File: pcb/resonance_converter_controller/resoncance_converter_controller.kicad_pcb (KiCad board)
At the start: 2 copper layers, 61.4 x 94 mm, 232 parts, among them J1 Micro_SD_Card_Det2, J2 USB_C_Receptacle_USB2.0_14P, J3 FX18-120P-0.8SV, J7 Conn_ARM_SWD_TagConnect_TC2030, Q1 FDMC8032L, Q2 FDMC8032L, Q3 SiR696DP, SW1 SW_SPST, U1 BQ25792RQMR, U10 INA280A1xDCK, U11 INA280A1xDCK, U12 INA280A1xDCK, U13 STM32G474VEHx, U14 APS6404L-SQRx-ZR, U15 APS6404L-SQRx-ZR, U16 AT24CS32-XHM, U17 TL3116, U18 OPA2356xxDGK, U19 OPA2325, U2 TPS55289RYQR, U20 OPA356xxDBV, U3 TPS54240DRC, U4 TPS73733DCQR, U5 OPA2325, U6 LP5907MFX-3.3, U7 OPA2356xxDGK, U8 OPA356xxDBV, U9 INA280A1xDCK, Y1 16Mhz

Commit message: Update conector in som
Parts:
- removed J3: FX18-120P-0.8SV, FX18-120P-0.8SV:HIROSE_FX18-120P-0.8SV
- added C90: 100nF, Capacitor_SMD:C_0402_1005Metric, F.Cu at (229.0, 79.0)
- added C91: 10uF, Capacitor_SMD:C_1206_3216Metric, F.Cu at (223.4, 82.4)
- added C92: 100nF, Capacitor_SMD:C_0402_1005Metric, F.Cu at (229.0, 80.9)
- added C93: 100nF, Capacitor_SMD:C_0402_1005Metric, F.Cu at (229.0, 82.9)
- added D25: ESD9B3.3ST5G, Diode_SMD:D_SOD-923, F.Cu at (233.9, 73.0)
- added D26: ESD9B3.3ST5G, Diode_SMD:D_SOD-923, F.Cu at (233.9, 74.9)
- added D27: ESD9B3.3ST5G, Diode_SMD:D_SOD-923, F.Cu at (233.9, 76.9)
- added D28: ESD9B3.3ST5G, Diode_SMD:D_SOD-923, F.Cu at (233.9, 78.8)
- added D29: ESD9B3.3ST5G, Diode_SMD:D_SOD-923, F.Cu at (233.9, 80.8)
- added D30: ESD9B3.3ST5G, Diode_SMD:D_SOD-923, F.Cu at (236.6, 73.0)
- added D31: ESD9B3.3ST5G, Diode_SMD:D_SOD-923, F.Cu at (236.6, 74.9)
- added D32: ESD9B3.3ST5G, Diode_SMD:D_SOD-923, F.Cu at (236.6, 76.9)
- added D33: ESD9B3.3ST5G, Diode_SMD:D_SOD-923, F.Cu at (236.6, 78.8)
- added D34: ESD9B3.3ST5G, Diode_SMD:D_SOD-923, F.Cu at (236.6, 80.8)
- added J4: Conn_02x19_Odd_Even, Connector_PinSocket_2.54mm:PinSocket_2x19_P2.54mm_Vertical_SMD, F.Cu at (209.9, 142.6)
- added J5: Conn_01x02, Connector_AMASS:AMASS_XT30U-M_1x02_P5.0mm_Vertical, F.Cu at (193.6, 155.8)
- added J6: FX18-120S-0.8SH, FX18-120S-0.8SH:HIROSE_FX18-120S-0.8SH, B.Cu at (209.2, 149.0)
- added R67: 0R, Resistor_SMD:R_0402_1005Metric, F.Cu at (229.0, 73.0)
- added R68: 240K, Resistor_SMD:R_0402_1005Metric, F.Cu at (229.0, 75.0)
- added R69: 100K, Resistor_SMD:R_0402_1005Metric, F.Cu at (229.0, 77.0)
- added R70: R, Resistor_SMD:R_0402_1005Metric, F.Cu at (239.3, 75.0)
- added R71: R, Resistor_SMD:R_2512_6332Metric, F.Cu at (194.3, 163.8)
- added RV1: 20K, Potentiometer_SMD:Potentiometer_Bourns_3269W_Vertical, F.Cu at (236.4, 88.4)
- added U21: TPS2553DRVR, TPS2553DRVR:SON65P200X200X80-7N, F.Cu at (214.4, 92.3)
- C84: value 100nF -> 100uF; footprint Capacitor_SMD:C_0805_2012Metric -> Capacitor_SMD:C_1206_3216Metric; moved to F.Cu
- R30: value 10K -> R
- moved R30 69.2 mm to (239.3, 73.0), turned to 0 degrees
- moved C84 28.4 mm to (223.4, 75.5), turned to 0 degrees
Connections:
- net SDA renamed I2C_INT_SDA
- net VPP renamed VSYS
- C84 pad 1: VCC -> Net-(J1-VDD)
- J1 pad 4: VCC -> Net-(J1-VDD)
- R30 pad 1: Net-(U5A--) -> /Controller/AUX_PWM_CH1
- R30 pad 2: GND -> AUX_PWM_CH1
- R39 pad 1: VCC -> Net-(J1-VDD)
- R40 pad 2: VCC -> Net-(J1-VDD)
- R6 pad 1: /Power supply/VOUT_ENABLE -> /Controller/VOUT_ENABLE
- U13 pad A1: LCD_SS -> SD_SS
- U13 pad A10: SD_MOSI -> LCD_MOSI
- U13 pad A5: unconnected-(U13-PB3-PadA5) -> HRTIM_EEV9
- U13 pad A6: QSPI_BK2_IO2 -> AUX_RX
- U13 pad A7: QSPI_BK2_IO1 -> AUX_TX
- U13 pad A9: unconnected-(U13-PD1-PadA9) -> LCD_DC
- U13 pad B1: /Controller/LCD_MISO -> SD_MOSI
- U13 pad B2: unconnected-(U13-PE3-PadB2) -> ENCODER_CHB
- U13 pad B3: unconnected-(U13-PE1-PadB3) -> CTRL_RX
- U13 pad B4: unconnected-(U13-PB7-PadB4) -> SD_CARD_DETECT
- U13 pad B7: unconnected-(U13-PD2-PadB7) -> LCD_RST
- U13 pad B8: unconnected-(U13-PD0-PadB8) -> LCD_BL
- U13 pad B9: SD_SS -> LCD_SS
- U13 pad C1: unconnected-(U13-PC14-PadC1) -> /INT
- U13 pad C2: LCD_MOSI -> SD_MISO
- U13 pad C3: LCD_SCK -> SD_SCK
- U13 pad C4: unconnected-(U13-PE0-PadC4) -> CTRL_TX
- U13 pad C6: unconnected-(U13-PD3-PadC6) -> QSPI_NCS
- U13 pad C7: SD_MISO -> LCD_MISO
- U13 pad C8: SD_SCK -> LCD_SCK
- U13 pad D1: unconnected-(U13-PC15-PadD1) -> /Controller/VOUT_ENABLE
- U13 pad F1: /Analog preprocess/FB_OCD2_RECTIFIED -> QSPI_BK2_IO1
- U13 pad F4: /Analog preprocess/ISENSE_3_OUT -> /Analog preprocess/ISENSE_4_OUT
- U13 pad G1: unconnected-(U13-PC3-PadG1) -> QSPI_BK2_IO2
- U13 pad G10: unconnected-(U13-PD15-PadG10) -> GPIO3
- U13 pad G2: unconnected-(U13-PA1-PadG2) -> /Controller/AUX_PWM_CH2
- U13 pad G4: unconnected-(U13-PA0-PadG4) -> /Controller/AUX_PWM_CH1
- U13 pad G5: /Analog preprocess/ISENSE_4_OUT -> /Analog preprocess/ISENSE_2_OUT
- U13 pad G7: unconnected-(U13-PD10-PadG7) -> GPIO0
- U13 pad G8: unconnected-(U13-PD9-PadG8) -> GPIO1
- U13 pad G9: unconnected-(U13-PD13-PadG9) -> GPIO2
- U13 pad H1: QSPI_NCS -> VSENSE_IN
- U13 pad H3: /Analog preprocess/ISENSE_2_OUT -> /Analog preprocess/ISENSE_1_OUT
- U13 pad H5: LCD_BL -> GPIO4
- U13 pad H6: LCD_DC -> GPIO5
- U13 pad J10: VSENSE_IN -> /Analog preprocess/FB_OCD2_RECTIFIED
- U13 pad J2: unconnected-(U13-PA6-PadJ2) -> FAN_PWM
- U13 pad J3: CTRL_RX -> unconnected-(U13-PC5-PadJ3)
- U13 pad J4: unconnected-(U13-PB2-PadJ4) -> ENCODER_CHA
- U13 pad J6: unconnected-(U13-PE11-PadJ6) -> GPIO6
- U13 pad J8: unconnected-(U13-PB10-PadJ8) -> HRTIM_FLT3
- U13 pad K2: CTRL_TX -> unconnected-(U13-PC4-PadK2)
- U13 pad K3: /Analog preprocess/ISENSE_1_OUT -> /Analog preprocess/ISENSE_3_OUT
- U13 pad K6: LCD_RST -> GPIO7
- U2 pad 1: /Power supply/VOUT_ENABLE -> /Controller/VOUT_ENABLE

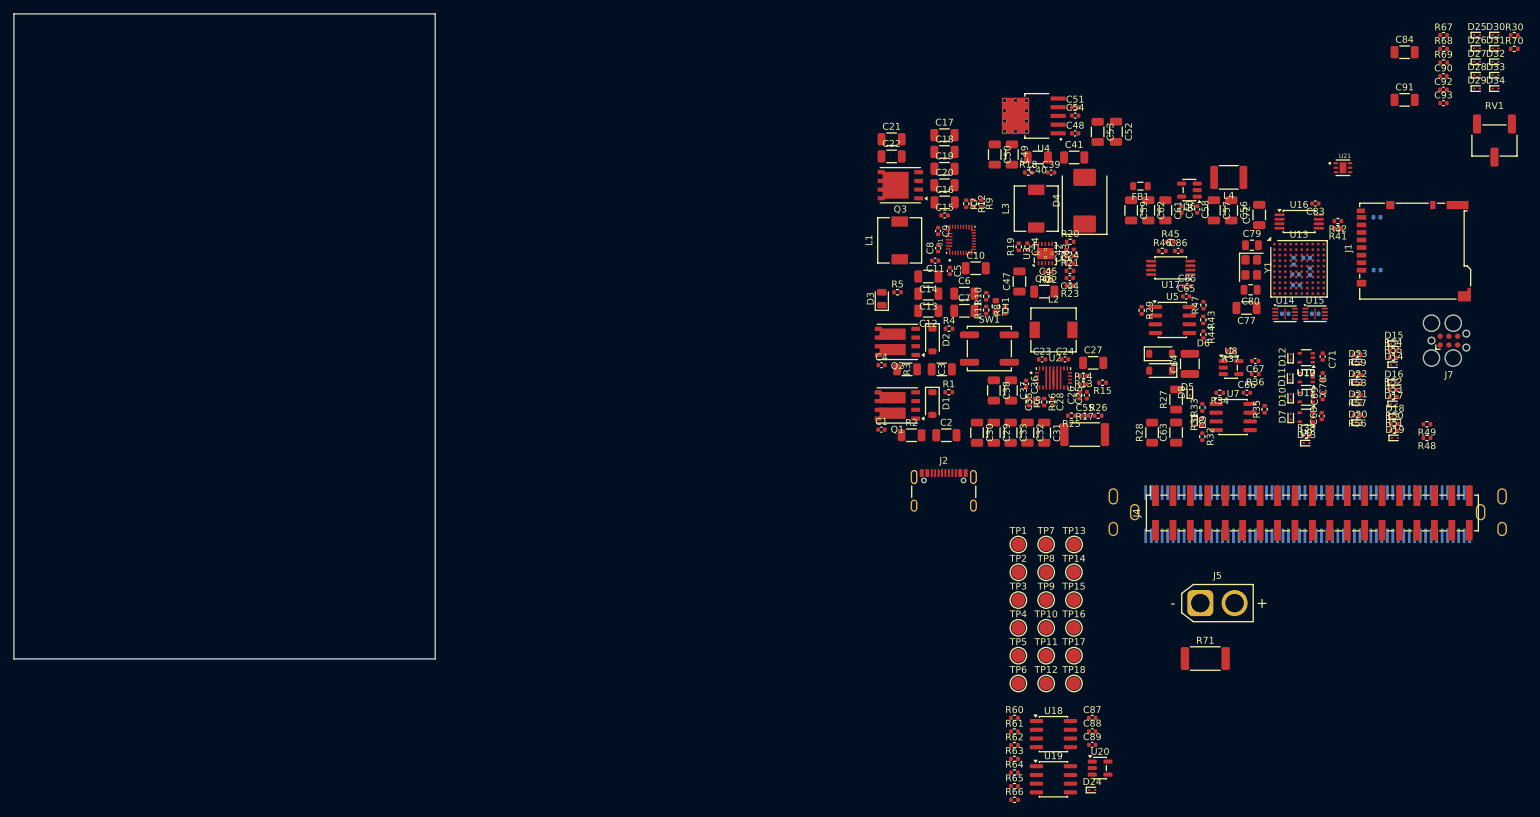
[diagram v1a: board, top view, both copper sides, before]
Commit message: First routing without testpoints
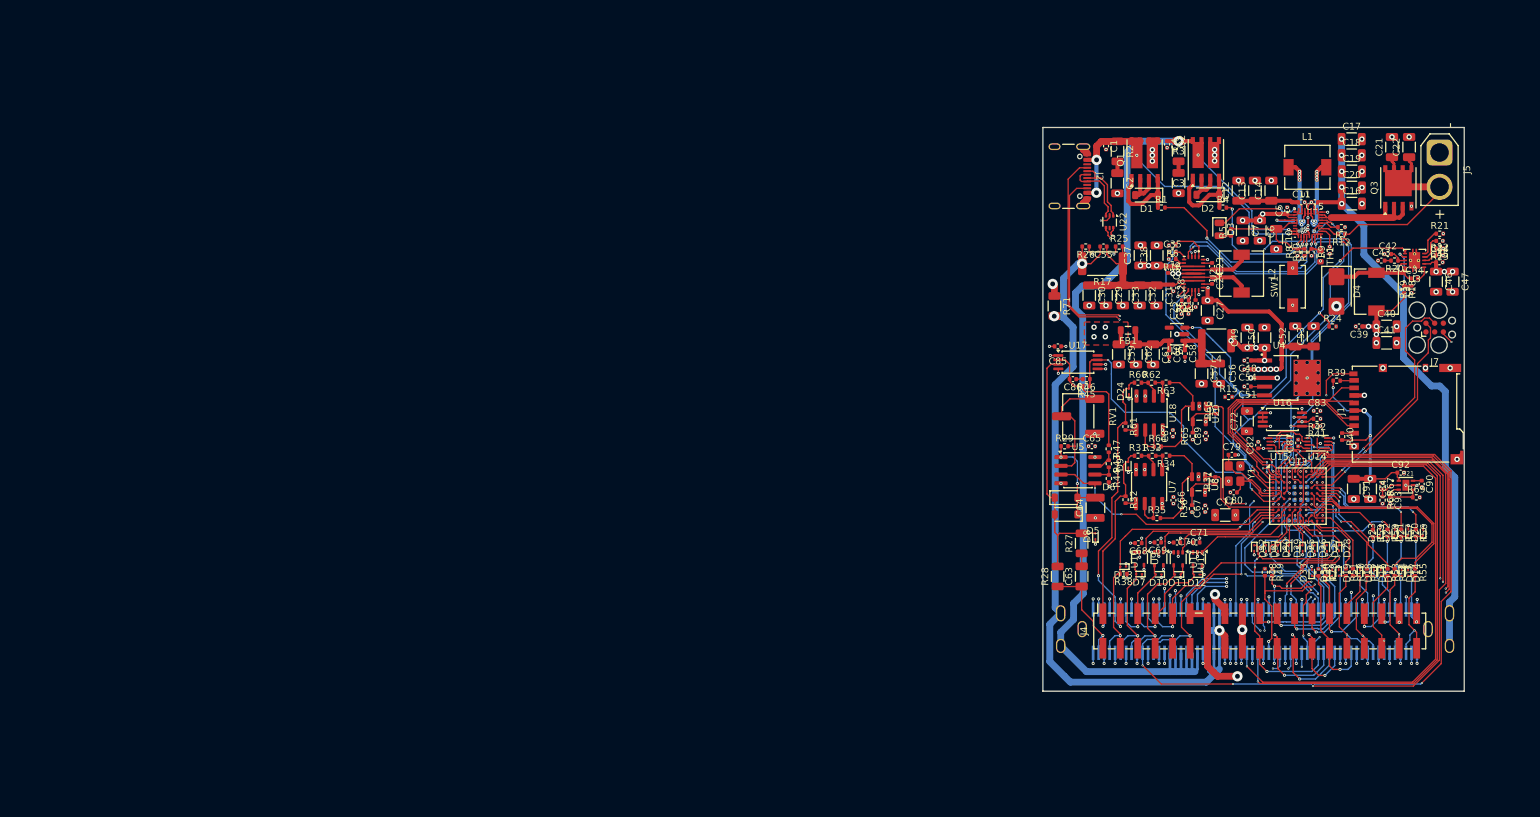
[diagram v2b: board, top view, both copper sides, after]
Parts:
- removed C88: 100nF, Capacitor_SMD:C_0402_1005Metric
- removed TP1, TP10, TP11, TP12, TP13, TP14, TP15, TP16, TP17, TP18, TP2, TP3, TP4, TP5, TP6, TP7, TP8, TP9: TestPoint_Probe, TestPoint:TestPoint_Pad_D2.0mm
- removed U19: OPA2325, Package_SO:SOIC-8_3.9x4.9mm_P1.27mm
- added U22: USBLC6-2P6, Package_TO_SOT_SMD:SOT-666, F.Cu at (180.4, 100.2)
- C79, C80: footprint Capacitor_SMD:C_0805_2012Metric -> Capacitor_SMD:C_0402_1005Metric
- C8, C9: moved to B.Cu
- C81, C82, R39, R40: moved to F.Cu
- D4: footprint Diode_SMD:D_SMC -> Diode_SMD:D_SMB
- R71: footprint Resistor_SMD:R_2512_6332Metric -> Resistor_SMD:R_1206_3216Metric
- SW1: footprint Button_Switch_SMD:SW_Push_1P1T_NO_CK_KSC6xxJ -> Button_Switch_SMD:SW_SPST_EVQPE1
- moved R30 83.3 mm to (210.8, 151.3), turned to -90 degrees
- moved D30 81.2 mm to (204.9, 147.8), turned to -90 degrees
- moved R70 81.1 mm to (211.8, 151.3), turned to -90 degrees
- moved D31 80.1 mm to (203.2, 147.8), turned to -90 degrees
- moved D32 79.1 mm to (201.4, 147.8), turned to -90 degrees
- moved D25 79.0 mm to (208.5, 147.8), turned to -90 degrees
- moved D33 77.3 mm to (209.8, 151.3), turned to 90 degrees
- moved D26 76.6 mm to (210.2, 147.8), turned to -90 degrees
- moved C22 75.4 mm to (224.0, 89.3), turned to 90 degrees
- moved D34 74.5 mm to (212.8, 151.4), turned to 90 degrees
- moved J5 74.3 mm to (228.4, 90.1), turned to -90 degrees
- moved D27 74.2 mm to (212.0, 147.8), turned to -90 degrees
- moved C21 72.9 mm to (221.5, 89.3), turned to 90 degrees
- moved RV1 72.8 mm to (175.8, 128.5), turned to -90 degrees
- moved Q3 72.6 mm to (222.4, 95.2), turned to 90 degrees
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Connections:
- net SCL renamed I2C_INT_SCL
- J2 pad A6: USB_DP -> /PUSB+
- J2 pad A7: USB_DM -> /PUSB-
- J2 pad B6: USB_DP -> /PUSB+
- J2 pad B7: USB_DM -> /PUSB-
- U13 pad C10: USB_DM -> USB_D-
- U13 pad C9: USB_DP -> USB_D+
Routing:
- net GND: track 0.00 -> 170.3 mm, vias 0 -> 239
- net VBUS_DOCK: track 0.00 -> 148.8 mm, vias 0 -> 3
- net VOUT: track 0.00 -> 129.5 mm, vias 0 -> 3
- net HRTIM_EEV9: track 0.00 -> 110.4 mm, vias 0 -> 6
- net VSYS: track 0.00 -> 104.4 mm, vias 0 -> 13
- net /INT: track 0.00 -> 87.5 mm, vias 0 -> 5
- net LCD_MISO: track 0.00 -> 82.5 mm, vias 0 -> 4
- net LCD_SCK: track 0.00 -> 79.6 mm, vias 0 -> 4
- net LCD_SS: track 0.00 -> 76.9 mm, vias 0 -> 1
- net LCD_MOSI: track 0.00 -> 76.5 mm, vias 0 -> 1
- net LCD_RST: track 0.00 -> 75.6 mm, vias 0 -> 2
- net I2C_INT_SCL: track 0.00 -> 72.7 mm, vias 0 -> 6
- net I2C_INT_SDA: track 0.00 -> 71.7 mm, vias 0 -> 6
- net CC1: track 0.00 -> 66.1 mm, vias 0 -> 2
- net USB_D+: track 0.00 -> 63.5 mm, vias 0 -> 2
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- added copper zone on In2.Cu, net +3.3VP
- added copper zone on F.Cu, net GND
- added copper zone on In1.Cu, net GND
- added copper zone on In4.Cu, net GND
- added copper zone on F.Cu, net VAA
- added copper zone on In2.Cu, net VAA
- added copper zone on In2.Cu, net VBUS
- added copper zone on In2.Cu, net VCC
- added copper zone on In2.Cu, net VSYS
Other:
- board size 61.4 x 94 mm -> 61.4 x 82.1 mm
- copper layers 2 -> 6

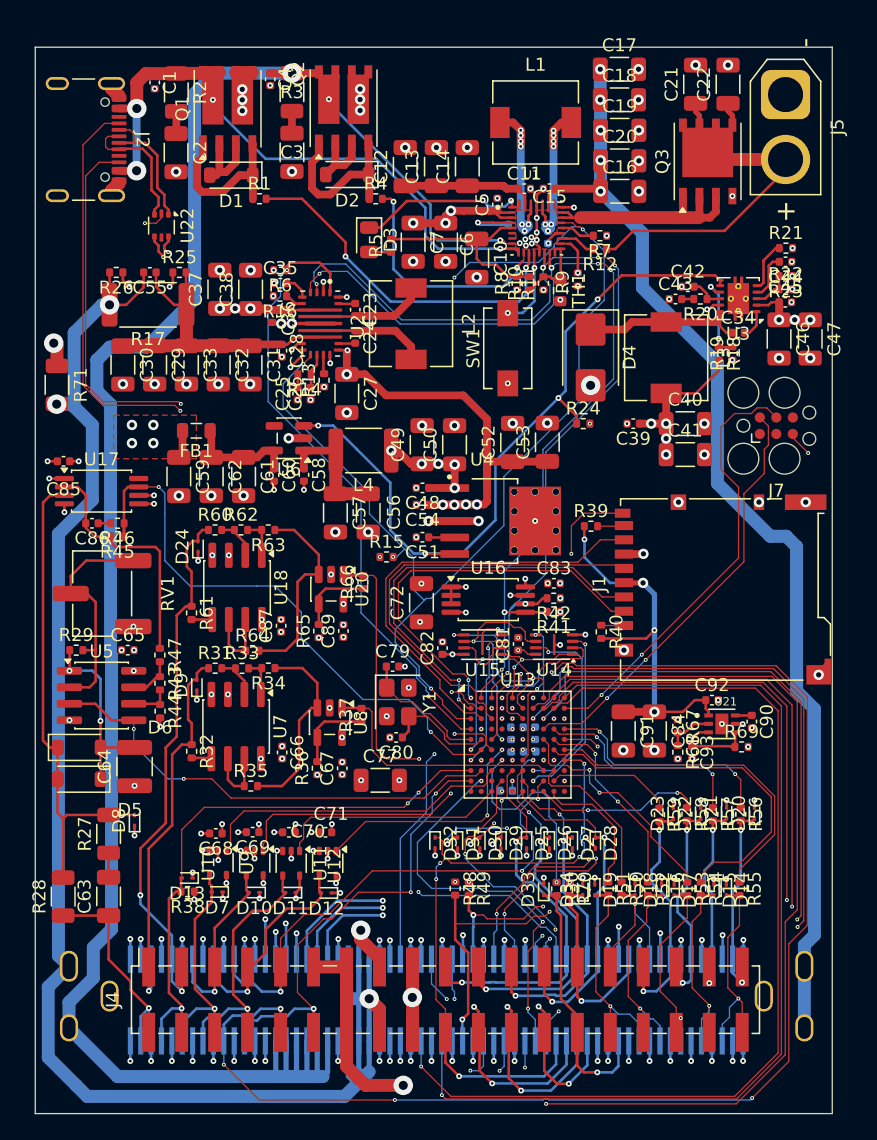
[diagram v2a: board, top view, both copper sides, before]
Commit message: Add mounting holes and some rework
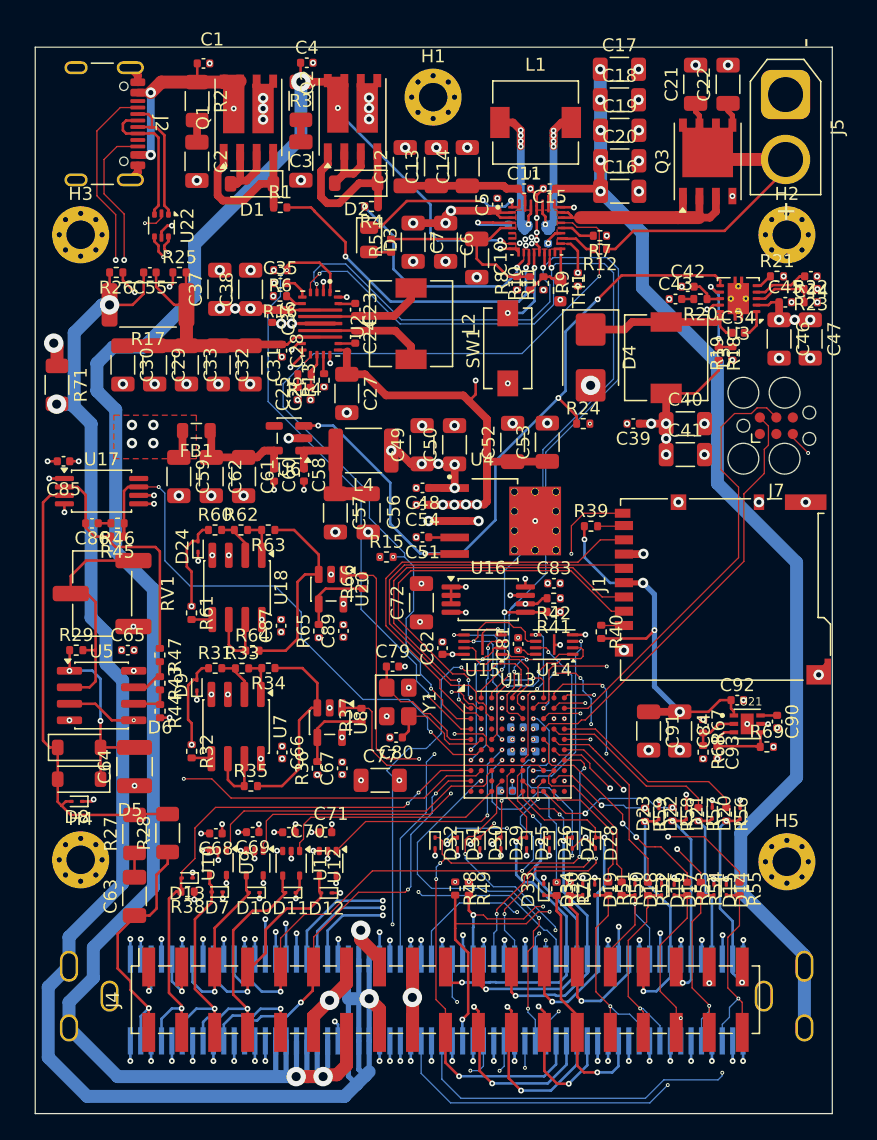
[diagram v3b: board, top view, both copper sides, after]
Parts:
- added H1: MountingHole_Pad_MP, MountingHole:MountingHole_2.2mm_M2_Pad_Via, F.Cu at (201.3, 90.3)
- added H2: MountingHole_Pad_MP, MountingHole:MountingHole_2.2mm_M2_Pad_Via, F.Cu at (228.6, 100.9)
- added H3: MountingHole_Pad_MP, MountingHole:MountingHole_2.2mm_M2_Pad_Via, F.Cu at (174.2, 100.9)
- added H4: MountingHole_Pad_MP, MountingHole:MountingHole_2.2mm_M2_Pad_Via, F.Cu at (174.2, 149.1)
- added H5: MountingHole_Pad_MP, MountingHole:MountingHole_2.2mm_M2_Pad_Via, F.Cu at (228.6, 149.2)
- moved R28 9.42 mm to (180.8, 147.0)
- moved D8 4.69 mm to (173.8, 144.6), turned to 180 degrees
- moved C1 4.03 mm to (183.6, 87.7), turned to 0 degrees
- moved C4 3.09 mm to (191.6, 87.7), turned to 0 degrees
- moved R21 2.27 mm to (227.8, 104.1)
- moved C44 2.25 mm to (230.4, 104.1)
- moved R22 2.17 mm to (230.4, 106.1)
- moved R23 2.17 mm to (230.4, 105.1)
- moved C63 2.00 mm to (178.3, 151.9)
- moved R27 2.00 mm to (178.3, 147.1)
- moved C84 1.95 mm to (220.3, 139.1)
- moved C90 1.95 mm to (227.8, 138.4)
- moved C91 1.95 mm to (217.9, 139.1)
- moved U21 1.95 mm to (225.5, 138.6)
- moved C92 1.95 mm to (224.7, 136.8)
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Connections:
- J4 pad 11: GND -> DAC_OUT
- J4 pad 12: DAC_OUT -> GND
- J4 pad 14: GND -> VBUS_DOCK
- U22 pad 5: +3.3V -> VCC
- U4 pad 10: (no net) -> GND
- U4 pad 11: (no net) -> GND
- U4 pad 12: (no net) -> GND
- U4 pad 13: (no net) -> GND
- U4 pad 14: (no net) -> GND
- U4 pad 15: (no net) -> GND
- U4 pad 16: (no net) -> GND
- U4 pad 7: (no net) -> GND
- U4 pad 8: (no net) -> GND
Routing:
- net HRTIM_EEV9: track 110.4 -> 50.5 mm, vias 6 -> 3
- net LCD_MISO: track 82.5 -> 32.7 mm, vias 4 -> 3
- net VCC: track 62.4 -> 94.8 mm
- net LCD_SCK: track 79.6 -> 47.3 mm, vias 4 -> 2
- net LCD_DC: track 57.3 -> 30.6 mm, vias 2 -> 3
- net LCD_BL: track 57.7 -> 32.6 mm, vias 2 -> 5
- net /INT: track 87.5 -> 69.2 mm, vias 5 -> 4
- net LCD_SS: track 76.9 -> 61.0 mm, vias 1 -> 2
- net LCD_MOSI: track 76.5 -> 63.7 mm, vias 1 -> 2
- net /Controller/OUT_SYNC_3+: track 28.3 -> 16.5 mm, vias 0 -> 2
- net LCD_RST: track 75.6 -> 65.6 mm
- net GND: track 170.3 -> 163.5 mm, vias 239 -> 238
- net /Controller/OUT_SYNC_3-: track 25.4 -> 18.9 mm, vias 0 -> 2
- net VBUS_DOCK: track 148.8 -> 154.5 mm, vias 3 -> 5
- net DAC_OUT: track 36.3 -> 32.0 mm
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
